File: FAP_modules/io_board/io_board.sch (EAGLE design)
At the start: 80 parts, among them IC1 STM32F051C8T6, IC2 EPM240-T100, IC3 24C08BSN, U2 OSCILLATORSMD

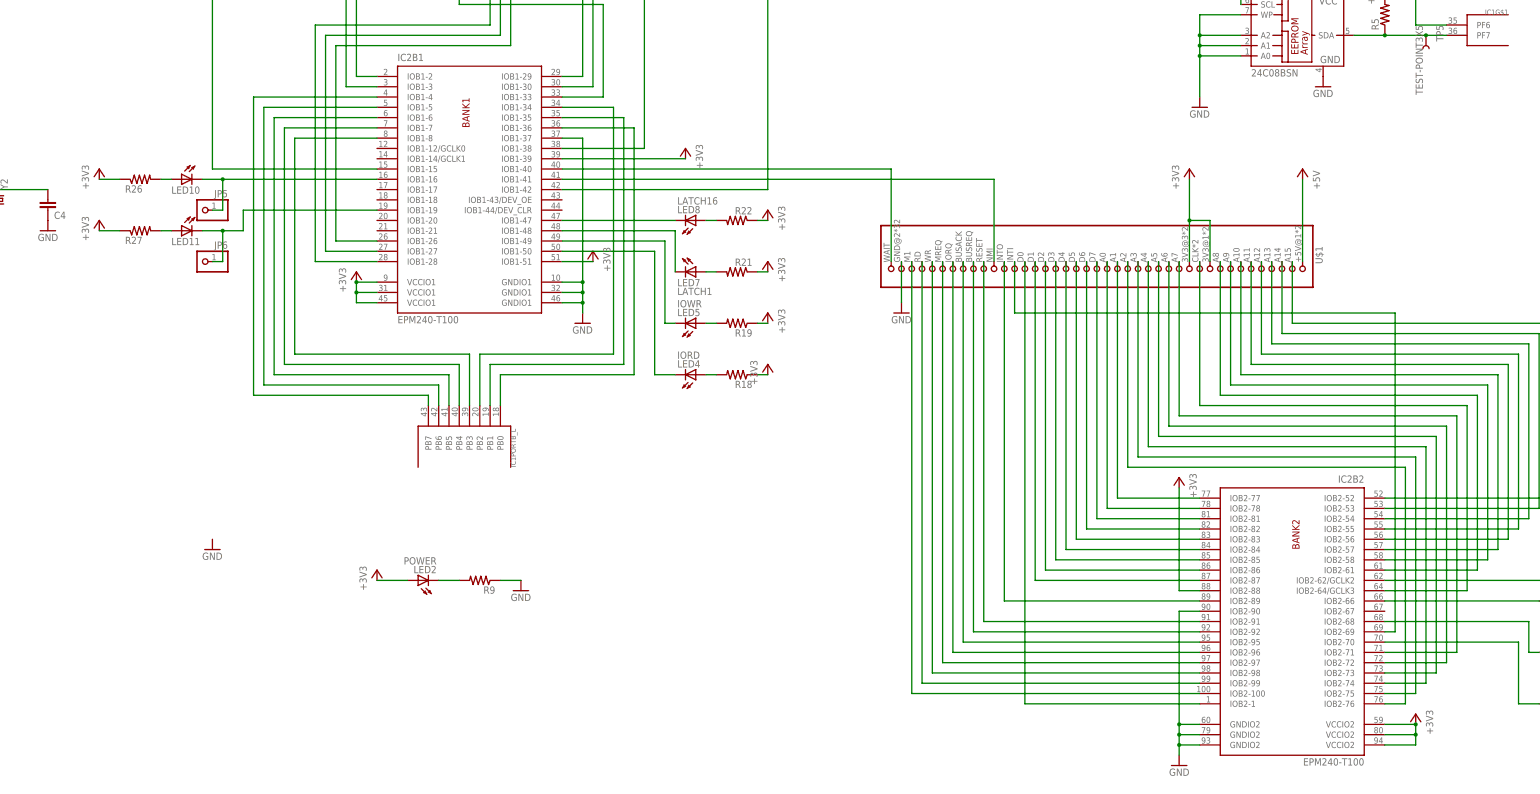
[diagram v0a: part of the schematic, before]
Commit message: added all Z80 signals on bus
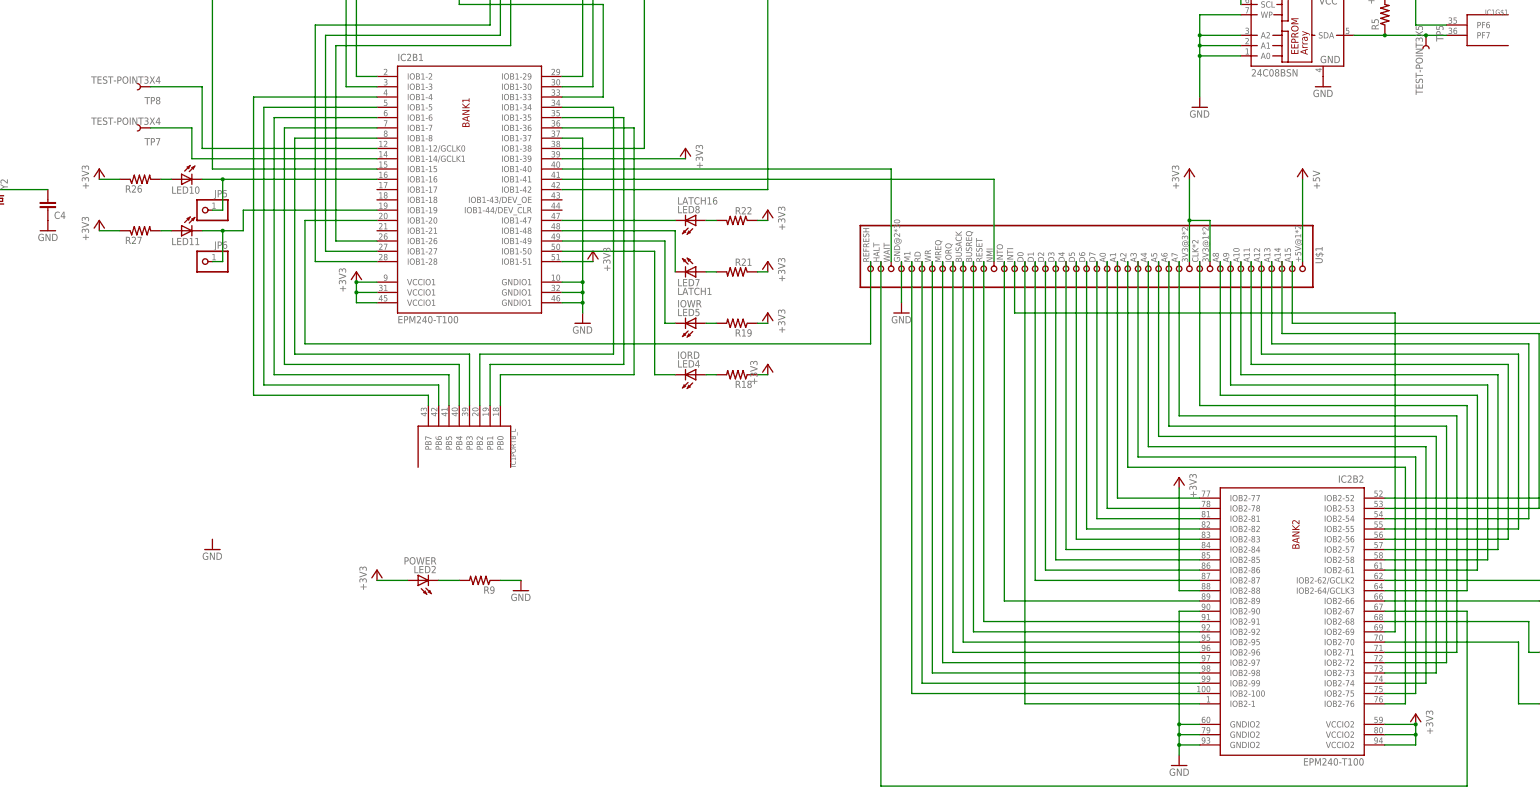
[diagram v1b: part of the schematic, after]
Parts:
- added TP7, TP8: TEST-POINT3X4, SparkFun-Passives:TEST-POINT3X4
- U$1: value FAP_BUS_FAP_BUS -> FAP_BUS; device cpu_board:FAP_BUS_FAP_BUS -> fap_bus:FAP_BUS
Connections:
- new net N$1: IC2B2.IOB2-67, U$1.41
- new net N$3: IC2B1.IOB1-20, U$1.42
- new net N$4: IC2B1.IOB1-12/GCLK0, TP8.1
- new net N$98: IC2B1.IOB1-14/GCLK1, TP7.1
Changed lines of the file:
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@@
 <part name="IC1" library="stm32f051" deviceset="STM32F051C8T6" device=""/>
 <part name="IC2" library="altera-max2" deviceset="EPM240-T100" device=""/>
-<part name="U$1" library="cpu_board" deviceset="FAP_BUS_FAP_BUS" device=""/>
+<part name="U$1" library="fap_bus" deviceset="FAP_BUS" device=""/>
 <part name="U$2" library="ps2" deviceset="PS/2" device=""/>
 <part name="Y1" library="SparkFun-FreqCtrl" deviceset="CRYSTAL" device="HC49US"/>
@@
 <part name="+3V42" library="supply1" deviceset="+3V3" device=""/>
 <part name="JP6" library="pinhead" deviceset="PINHD-1X1" device=""/>
+<part name="TP7" library="SparkFun-Passives" deviceset="TEST-POINT" device="3X4" value="TEST-POINT3X4"/>
+<part name="TP8" library="SparkFun-Passives" deviceset="TEST-POINT" device="3X4" value="TEST-POINT3X4"/>
 </parts>
 <sheets>
@@
 <instance part="+3V42" gate="G$1" x="-121.92" y="-116.84"/>
 <instance part="JP6" gate="G$1" x="-96.52" y="-127" rot="MR0"/>
+<instance part="TP7" gate="G$1" x="-109.22" y="-93.98" rot="R180"/>
+<instance part="TP8" gate="G$1" x="-109.22" y="-83.82" rot="R180"/>
 </instances>
 <busses>
@@
 </segment>
 </net>
+<net name="N$1" class="0">
+<segment>
+<pinref part="U$1" gate="G$1" pin="41"/>
+<wire x1="71.12" y1="-127" x2="71.12" y2="-256.54" width="0.1524" layer="91"/>
+<wire x1="71.12" y1="-256.54" x2="215.9" y2="-256.54" width="0.1524" layer="91"/>
+<pinref part="IC2" gate="B2" pin="IOB2-67"/>
+<wire x1="215.9" y1="-256.54" x2="215.9" y2="-213.36" width="0.1524" layer="91"/>
+<wire x1="215.9" y1="-213.36" x2="195.58" y2="-213.36" width="0.1524" layer="91"/>
+</segment>
+</net>
+<net name="N$3" class="0">
+<segment>
+<pinref part="IC2" gate="B1" pin="IOB1-20"/>
+<wire x1="-53.34" y1="-116.84" x2="-71.12" y2="-116.84" width="0.1524" layer="91"/>
+<wire x1="-71.12" y1="-116.84" x2="-71.12" y2="-147.32" width="0.1524" layer="91"/>
+<wire x1="-71.12" y1="-147.32" x2="68.58" y2="-147.32" width="0.1524" layer="91"/>
+<pinref part="U$1" gate="G$1" pin="42"/>
+<wire x1="68.58" y1="-147.32" x2="68.58" y2="-127" width="0.1524" layer="91"/>
+</segment>
+</net>
+<net name="N$4" class="0">
+<segment>
+<pinref part="IC2" gate="B1" pin="IOB1-12/GCLK0"/>
+<wire x1="-53.34" y1="-99.06" x2="-96.52" y2="-99.06" width="0.1524" layer="91"/>
+<wire x1="-96.52" y1="-99.06" x2="-96.52" y2="-83.82" width="0.1524" layer="91"/>
+<pinref part="TP8" gate="G$1" pin="1"/>
+<wire x1="-96.52" y1="-83.82" x2="-109.22" y2="-83.82" width="0.1524" layer="91"/>
+</segment>
+</net>
+<net name="N$98" class="0">
+<segment>
+<pinref part="IC2" gate="B1" pin="IOB1-14/GCLK1"/>
+<wire x1="-53.34" y1="-101.6" x2="-99.06" y2="-101.6" width="0.1524" layer="91"/>
+<wire x1="-99.06" y1="-101.6" x2="-99.06" y2="-93.98" width="0.1524" layer="91"/>
+<pinref part="TP7" gate="G$1" pin="1"/>
+<wire x1="-99.06" y1="-93.98" x2="-109.22" y2="-93.98" width="0.1524" layer="91"/>
+</segment>
+</net>

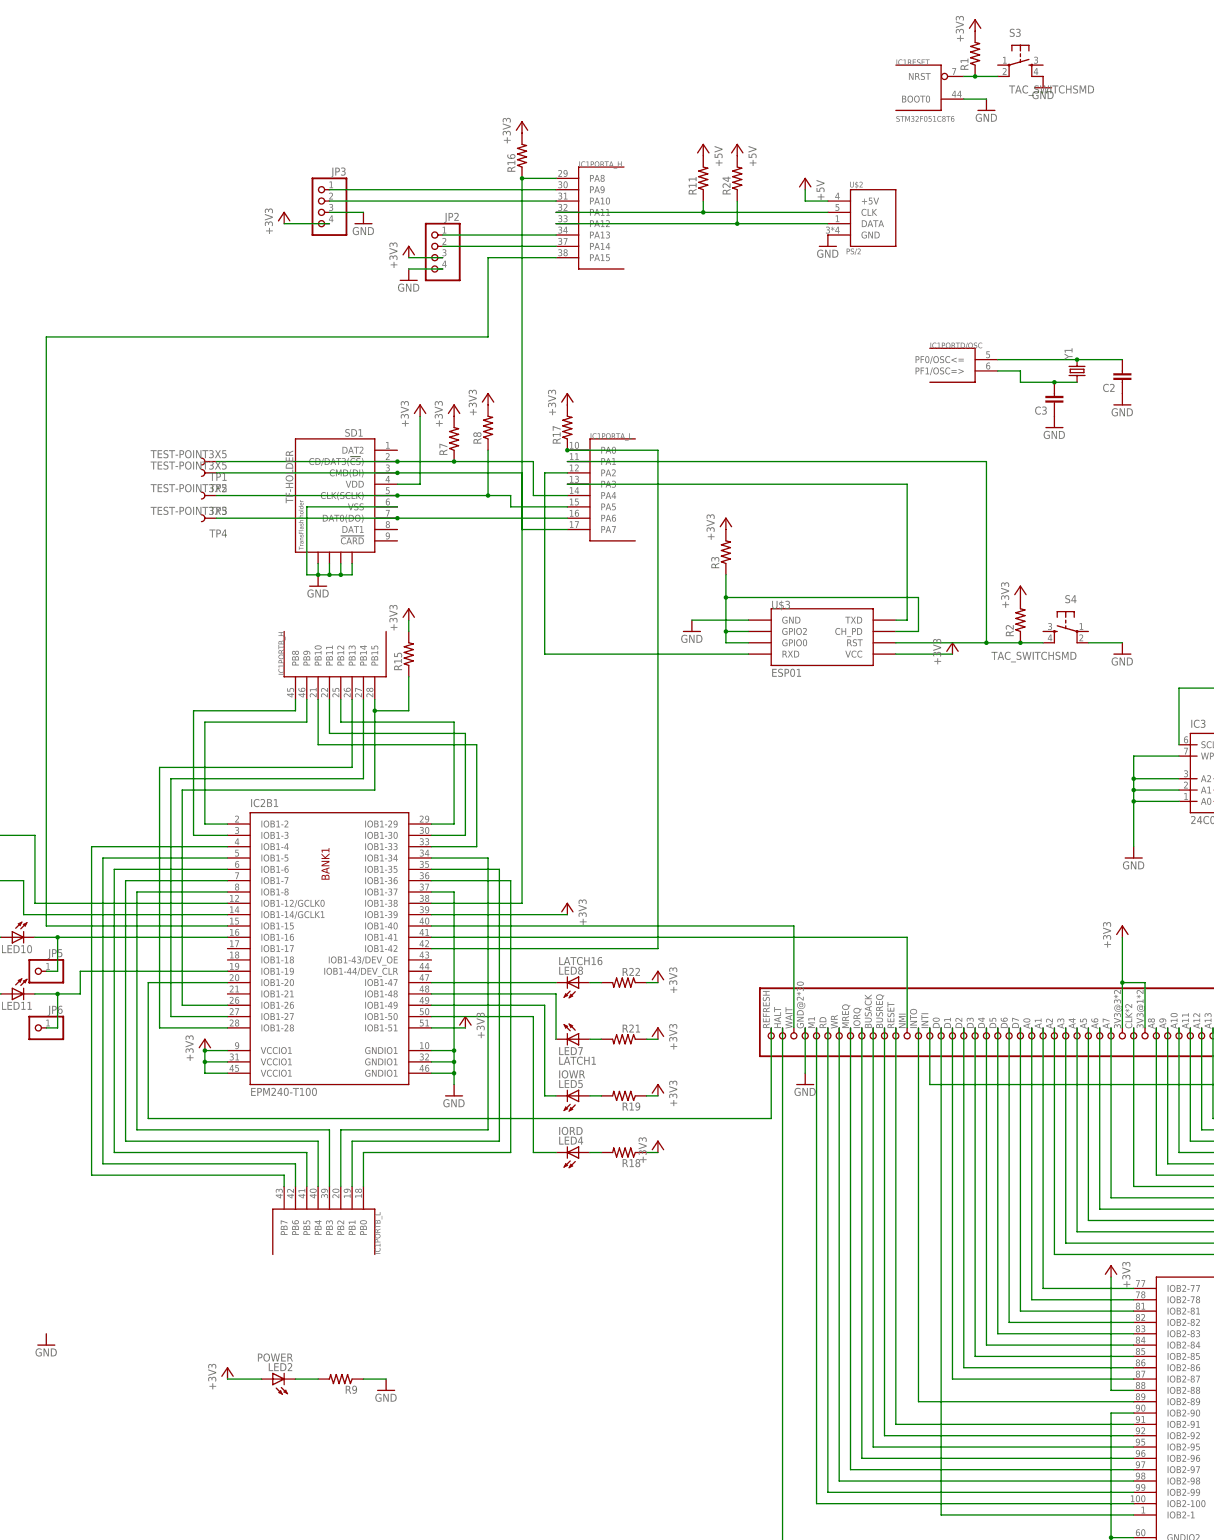
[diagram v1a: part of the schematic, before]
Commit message: connected BUSREQ to CPLD DEV_OE
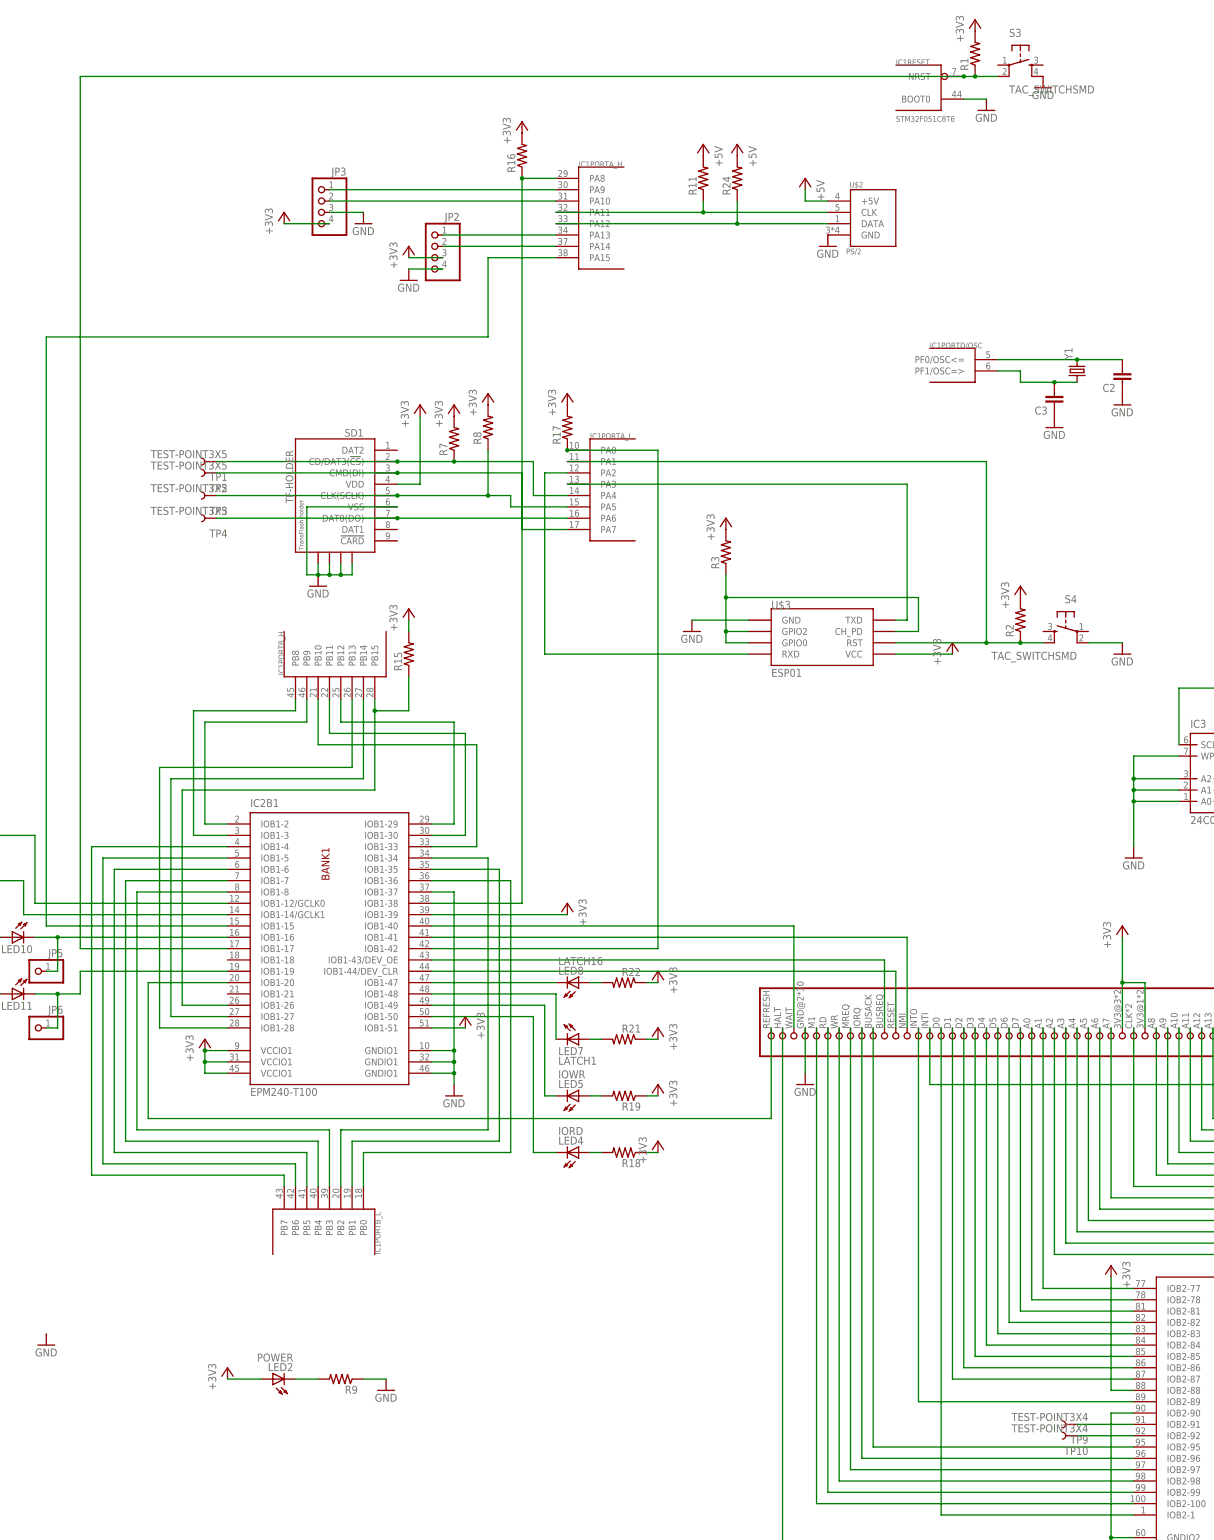
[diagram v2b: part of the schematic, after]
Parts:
- added TP10, TP9: TEST-POINT3X4, SparkFun-Passives:TEST-POINT3X4
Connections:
- new net N$106: IC2B2.IOB2-91, TP9.1
- new net N$107: IC2B2.IOB2-92, TP10.1
- net N$14: now also IC2B1.IOB1-43/DEV_OE; no longer IC2B2.IOB2-92
- net N$21: now also IC2B1.IOB1-44/DEV_CLR; no longer IC2B2.IOB2-91
- net N$5: now also IC2B1.IOB1-17
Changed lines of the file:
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@@
 <part name="TP7" library="SparkFun-Passives" deviceset="TEST-POINT" device="3X4" value="TEST-POINT3X4"/>
 <part name="TP8" library="SparkFun-Passives" deviceset="TEST-POINT" device="3X4" value="TEST-POINT3X4"/>
+<part name="TP9" library="SparkFun-Passives" deviceset="TEST-POINT" device="3X4" value="TEST-POINT3X4"/>
+<part name="TP10" library="SparkFun-Passives" deviceset="TEST-POINT" device="3X4" value="TEST-POINT3X4"/>
 </parts>
 <sheets>
@@
 <instance part="TP7" gate="G$1" x="-109.22" y="-93.98" rot="R180"/>
 <instance part="TP8" gate="G$1" x="-109.22" y="-83.82" rot="R180"/>
+<instance part="TP9" gate="G$1" x="137.16" y="-215.9" rot="R180"/>
+<instance part="TP10" gate="G$1" x="137.16" y="-218.44" rot="R180"/>
 </instances>
 <busses>
@@
 <junction x="114.3" y="86.36"/>
 <pinref part="S3" gate="S" pin="2"/>
+<pinref part="IC2" gate="B1" pin="IOB1-17"/>
+<wire x1="-53.34" y1="-109.22" x2="-86.36" y2="-109.22" width="0.1524" layer="91"/>
+<wire x1="-86.36" y1="-109.22" x2="-86.36" y2="86.36" width="0.1524" layer="91"/>
+<wire x1="-86.36" y1="86.36" x2="111.76" y2="86.36" width="0.1524" layer="91"/>
+<junction x="111.76" y="86.36"/>
 </segment>
 </net>
@@
 </segment>
 </net>
-<net name="N$14" class="0">
-<segment>
-<pinref part="U$1" gate="G$1" pin="32"/>
-<pinref part="IC2" gate="B2" pin="IOB2-92"/>
-<wire x1="93.98" y1="-127" x2="93.98" y2="-218.44" width="0.1524" layer="91"/>
-<wire x1="93.98" y1="-218.44" x2="149.86" y2="-218.44" width="0.1524" layer="91"/>
-</segment>
-</net>
 <net name="N$21" class="0">
 <segment>
 <pinref part="U$1" gate="G$1" pin="31"/>
-<pinref part="IC2" gate="B2" pin="IOB2-91"/>
-<wire x1="96.52" y1="-127" x2="96.52" y2="-215.9" width="0.1524" layer="91"/>
-<wire x1="96.52" y1="-215.9" x2="149.86" y2="-215.9" width="0.1524" layer="91"/>
+<pinref part="IC2" gate="B1" pin="IOB1-44/DEV_CLR"/>
+<wire x1="96.52" y1="-127" x2="96.52" y2="-114.3" width="0.1524" layer="91"/>
+<wire x1="96.52" y1="-114.3" x2="-7.62" y2="-114.3" width="0.1524" layer="91"/>
 </segment>
 </net>
@@
 </segment>
 </net>
+<net name="N$14" class="0">
+<segment>
+<pinref part="U$1" gate="G$1" pin="32"/>
+<pinref part="IC2" gate="B1" pin="IOB1-43/DEV_OE"/>
+<wire x1="93.98" y1="-127" x2="93.98" y2="-111.76" width="0.1524" layer="91"/>
+<wire x1="93.98" y1="-111.76" x2="-7.62" y2="-111.76" width="0.1524" layer="91"/>
+</segment>
+</net>
+<net name="N$106" class="0">
+<segment>
+<pinref part="IC2" gate="B2" pin="IOB2-91"/>
+<pinref part="TP9" gate="G$1" pin="1"/>
+<wire x1="149.86" y1="-215.9" x2="137.16" y2="-215.9" width="0.1524" layer="91"/>
+</segment>
+</net>
+<net name="N$107" class="0">
+<segment>
+<pinref part="IC2" gate="B2" pin="IOB2-92"/>
+<pinref part="TP10" gate="G$1" pin="1"/>
+<wire x1="149.86" y1="-218.44" x2="137.16" y2="-218.44" width="0.1524" layer="91"/>
+</segment>
+</net>

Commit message: firmware updates
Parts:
- added R28: (no value), SparkFun-Passives:RESISTOR0805-RES
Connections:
- new net N$108: R28.1, U$3.GPIO2
- net +3V3: now also R28.2, U$3.CH_PD
- net N$68: no longer U$3.CH_PD, U$3.GPIO2
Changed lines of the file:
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@@
 <part name="TP9" library="SparkFun-Passives" deviceset="TEST-POINT" device="3X4" value="TEST-POINT3X4"/>
 <part name="TP10" library="SparkFun-Passives" deviceset="TEST-POINT" device="3X4" value="TEST-POINT3X4"/>
+<part name="+3V43" library="supply1" deviceset="+3V3" device=""/>
+<part name="+3V44" library="supply1" deviceset="+3V3" device=""/>
+<part name="R28" library="SparkFun-Passives" deviceset="RESISTOR" device="0805-RES"/>
 </parts>
 <sheets>
@@
 <instance part="TP9" gate="G$1" x="137.16" y="-215.9" rot="R180"/>
 <instance part="TP10" gate="G$1" x="137.16" y="-218.44" rot="R180"/>
+<instance part="+3V43" gate="G$1" x="109.22" y="-30.48"/>
+<instance part="+3V44" gate="G$1" x="63.5" y="-12.7"/>
+<instance part="R28" gate="G$1" x="63.5" y="-20.32" rot="R90"/>
 </instances>
 <busses>
@@
 <wire x1="-121.92" y1="-119.38" x2="-116.84" y2="-119.38" width="0.1524" layer="91"/>
 </segment>
+<segment>
+<pinref part="U$3" gate="G$1" pin="CH_PD"/>
+<pinref part="+3V43" gate="G$1" pin="+3V3"/>
+<wire x1="96.52" y1="-38.1" x2="109.22" y2="-38.1" width="0.1524" layer="91"/>
+<wire x1="109.22" y1="-38.1" x2="109.22" y2="-33.02" width="0.1524" layer="91"/>
+</segment>
+<segment>
+<pinref part="+3V44" gate="G$1" pin="+3V3"/>
+<pinref part="R28" gate="G$1" pin="2"/>
+</segment>
 </net>
 <net name="N$5" class="0">
@@
 <segment>
 <pinref part="R3" gate="G$1" pin="1"/>
-<pinref part="U$3" gate="G$1" pin="GPIO2"/>
-<wire x1="58.42" y1="-25.4" x2="58.42" y2="-30.48" width="0.1524" layer="91"/>
-<wire x1="58.42" y1="-30.48" x2="58.42" y2="-38.1" width="0.1524" layer="91"/>
-<wire x1="58.42" y1="-38.1" x2="63.5" y2="-38.1" width="0.1524" layer="91"/>
+<wire x1="58.42" y1="-25.4" x2="58.42" y2="-40.64" width="0.1524" layer="91"/>
 <pinref part="U$3" gate="G$1" pin="GPIO0"/>
 <wire x1="63.5" y1="-40.64" x2="58.42" y2="-40.64" width="0.1524" layer="91"/>
-<wire x1="58.42" y1="-40.64" x2="58.42" y2="-38.1" width="0.1524" layer="91"/>
-<junction x="58.42" y="-38.1"/>
-<pinref part="U$3" gate="G$1" pin="CH_PD"/>
-<wire x1="96.52" y1="-38.1" x2="101.6" y2="-38.1" width="0.1524" layer="91"/>
-<wire x1="101.6" y1="-38.1" x2="101.6" y2="-30.48" width="0.1524" layer="91"/>
-<wire x1="101.6" y1="-30.48" x2="58.42" y2="-30.48" width="0.1524" layer="91"/>
-<junction x="58.42" y="-30.48"/>
 </segment>
 </net>
@@
 </segment>
 </net>
+<net name="N$108" class="0">
+<segment>
+<pinref part="U$3" gate="G$1" pin="GPIO2"/>
+<pinref part="R28" gate="G$1" pin="1"/>
+<wire x1="63.5" y1="-38.1" x2="63.5" y2="-25.4" width="0.1524" layer="91"/>
+</segment>
+</net>
